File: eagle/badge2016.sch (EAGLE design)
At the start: 89 parts, among them IC1 25AA080SN, IC3 24AA01SN, J1 USB-MICRO, Q1_32.768KHZ NX5032G, Q2 BC857ALT1SMD, Q2_24MHZ NX5032G, X1 PASSER-07, X2 PASSER-07, X3 PASSER-07

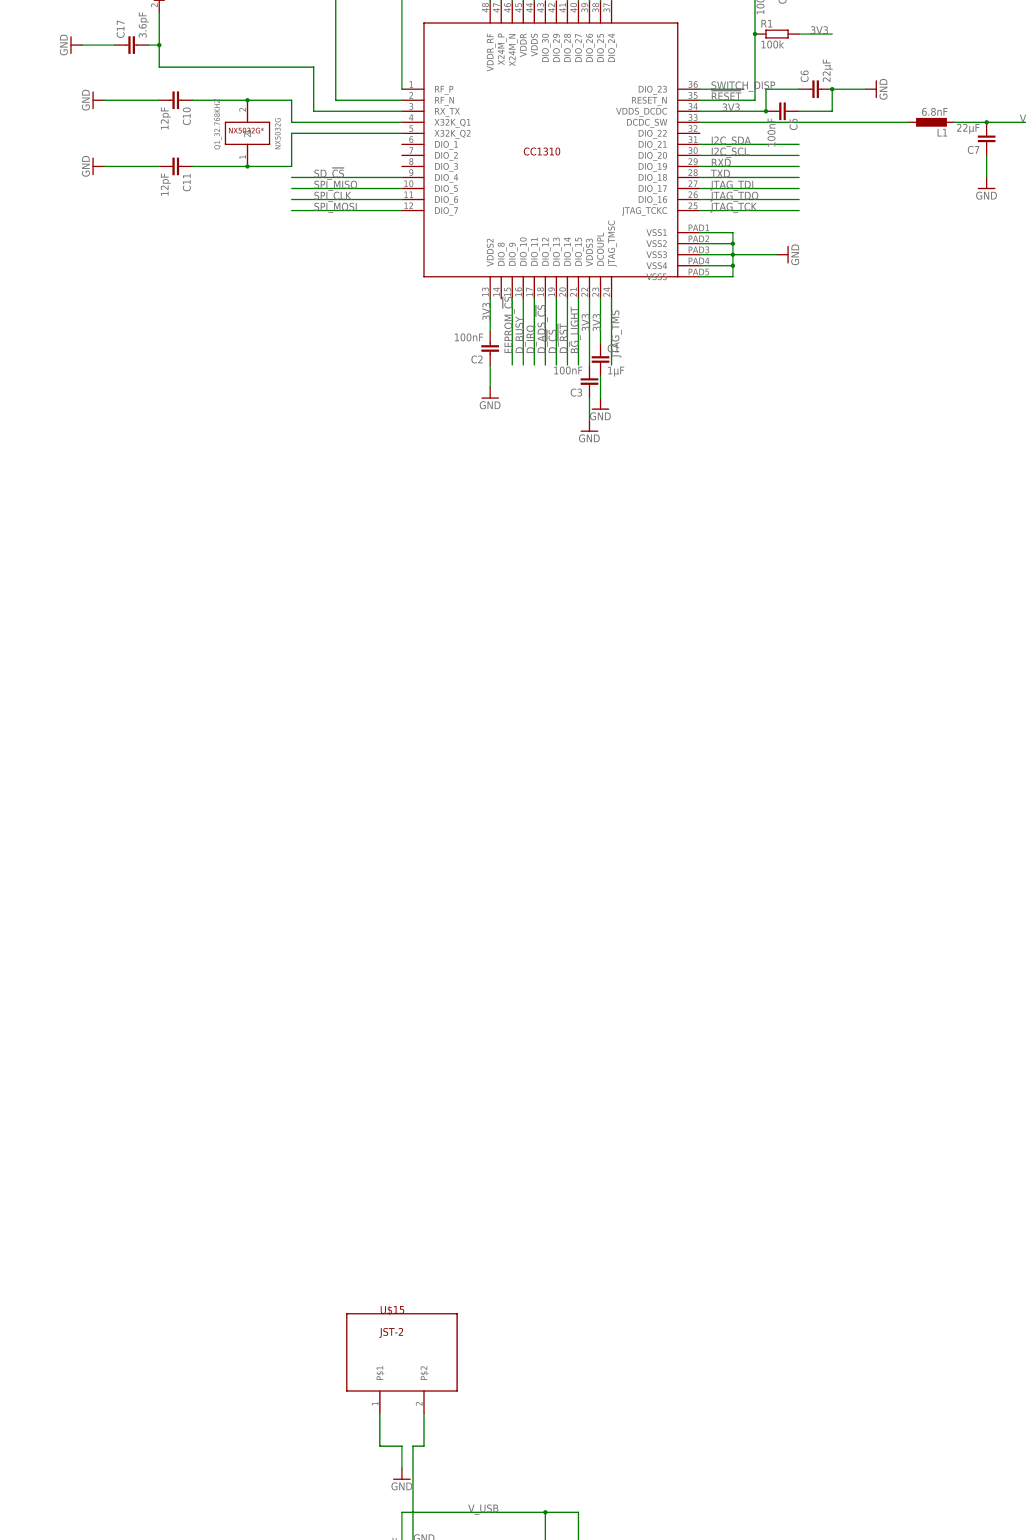
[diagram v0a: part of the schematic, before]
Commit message: fixed the inductor label (nF to nH) swapped 32khz crystal to different package + added package to lbr add pinhead to battery connector
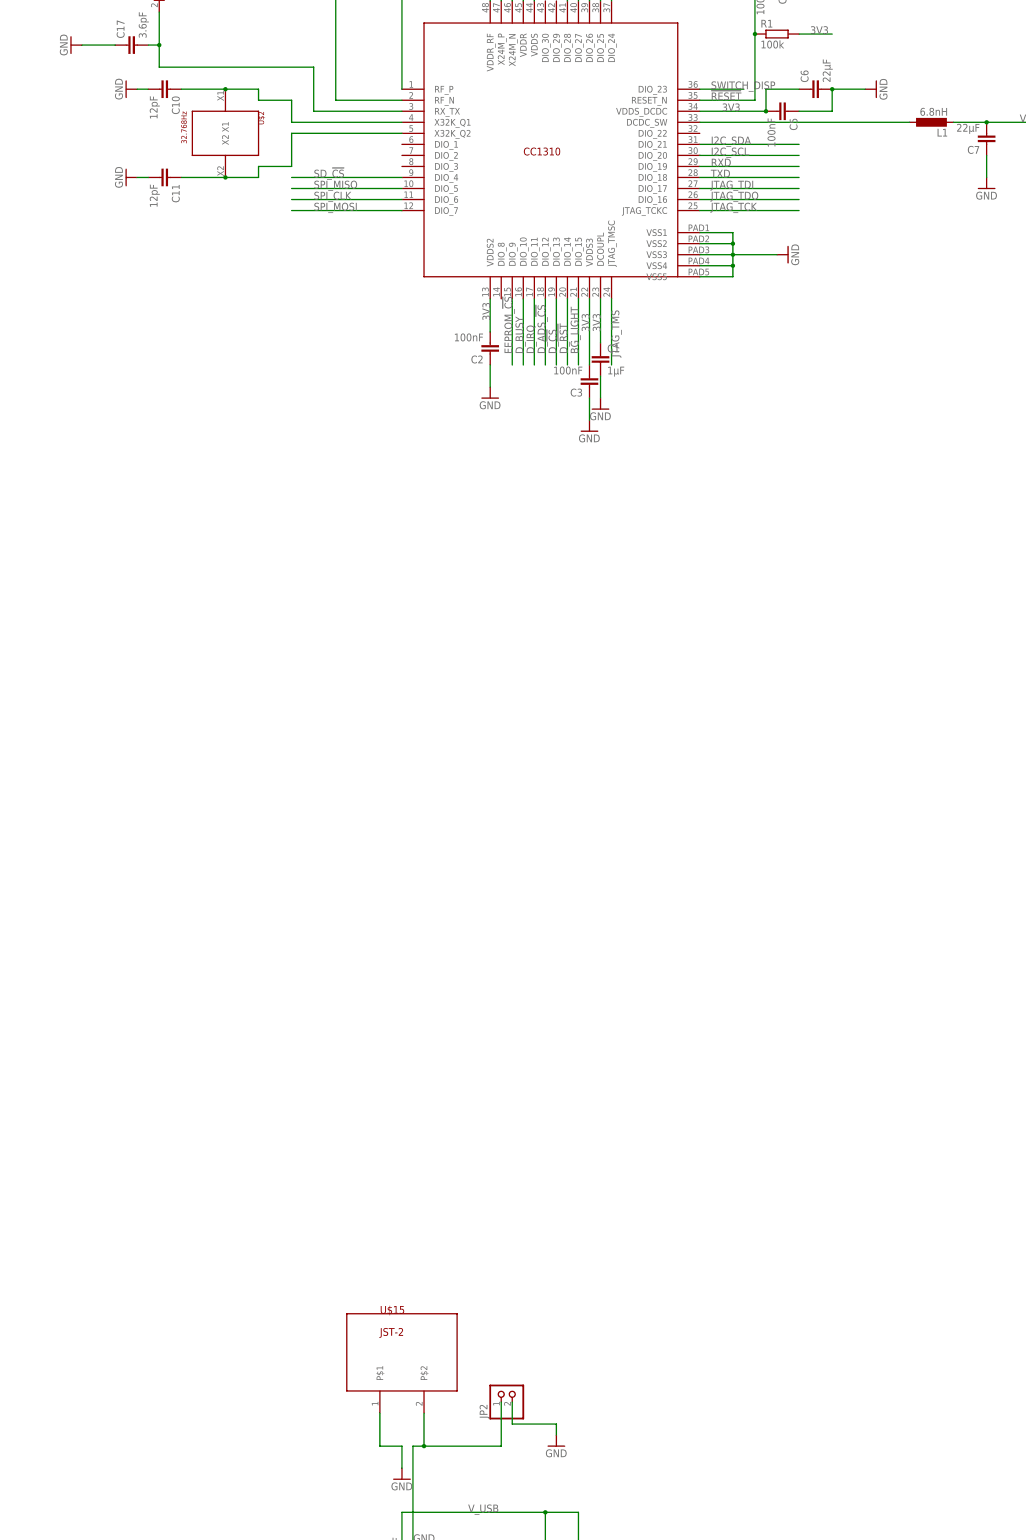
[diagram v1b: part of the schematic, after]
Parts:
- removed Q1_32.768KHZ: NX5032G, ERNW_parts:NX5032G
- added JP2: (no value), pinhead:PINHD-1X2
- added U$2: 32.768Hz, ERNW_parts:CMR200T
- L1: value 6.8nF -> 6.8nH
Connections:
- removed net N$1: C11.1, Q1_32.768KHZ.1, U$1.X32K_Q2
- new net N$16: C11.1, U$1.X32K_Q2, U$2.X2
- net GND: now also JP2.2
- net N$2: now also U$2.X1; no longer Q1_32.768KHZ.2
- net N$20: now also JP2.1
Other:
- moved on the sheet: C10, C11
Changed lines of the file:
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@@
 <part name="GND5" library="supply1" deviceset="GND" device=""/>
 <part name="GND6" library="supply1" deviceset="GND" device=""/>
-<part name="L1" library="rcl" deviceset="L-EU" device="L2012C" value="6.8nF"/>
+<part name="L1" library="rcl" deviceset="L-EU" device="L2012C" value="6.8nH"/>
 <part name="C6" library="rcl" deviceset="C-EU" device="C0603" value="22µF"/>
 <part name="C7" library="rcl" deviceset="C-EU" device="C0603" value="22µF"/>
@@
 <part name="GND8" library="supply1" deviceset="GND" device=""/>
 <part name="GND9" library="supply1" deviceset="GND" device=""/>
-<part name="Q1_32.768KHZ" library="ERNW_parts" deviceset="NX5032G*" device=""/>
 <part name="C10" library="rcl" deviceset="C-EU" device="C0402" value="12pF"/>
 <part name="C11" library="rcl" deviceset="C-EU" device="C0402" value="12pF"/>
@@
 <part name="R18" library="rcl" deviceset="R-EU_" device="R0402" value="NC"/>
 <part name="R21" library="rcl" deviceset="R-EU_" device="R0402" value="NC"/>
+<part name="U$2" library="ERNW_parts" deviceset="CMR200T" device="" value="32.768Hz"/>
+<part name="JP2" library="pinhead" deviceset="PINHD-1X2" device=""/>
+<part name="GND57" library="supply1" deviceset="GND" device=""/>
 </parts>
 <sheets>
@@
 <instance part="GND8" gate="1" x="43.18" y="104.14" rot="R180"/>
 <instance part="GND9" gate="1" x="50.8" y="116.84" rot="R180"/>
-<instance part="Q1_32.768KHZ" gate="G$1" x="-12.7" y="45.72" rot="R90"/>
-<instance part="C10" gate="G$1" x="-27.94" y="53.34" rot="R270"/>
-<instance part="C11" gate="G$1" x="-27.94" y="38.1" rot="R270"/>
-<instance part="GND10" gate="1" x="-48.26" y="53.34" rot="R270"/>
-<instance part="GND11" gate="1" x="-48.26" y="38.1" rot="R270"/>
+<instance part="C10" gate="G$1" x="-30.48" y="55.88" rot="R270"/>
+<instance part="C11" gate="G$1" x="-30.48" y="35.56" rot="R270"/>
+<instance part="GND10" gate="1" x="-40.64" y="55.88" rot="R270"/>
+<instance part="GND11" gate="1" x="-40.64" y="35.56" rot="R270"/>
 <instance part="Q2_24MHZ" gate="G$1" x="45.72" y="134.62" rot="R180"/>
 <instance part="C12" gate="G$1" x="38.1" y="157.48"/>
@@
 <instance part="R18" gate="G$1" x="226.06" y="-193.04" rot="R270"/>
 <instance part="R21" gate="G$1" x="233.68" y="-193.04" rot="R270"/>
+<instance part="U$2" gate="G$1" x="-17.78" y="45.72" rot="R270"/>
+<instance part="JP2" gate="G$1" x="48.26" y="-243.84" rot="R90"/>
+<instance part="GND57" gate="1" x="58.42" y="-256.54"/>
 </instances>
 <busses>
@@
 <pinref part="GND9" gate="1" pin="GND"/>
 <wire x1="50.8" y1="104.14" x2="50.8" y2="114.3" width="0.1524" layer="91"/>
-</segment>
-<segment>
-<pinref part="GND11" gate="1" pin="GND"/>
-<pinref part="C11" gate="G$1" pin="2"/>
-<wire x1="-45.72" y1="38.1" x2="-33.02" y2="38.1" width="0.1524" layer="91"/>
-</segment>
-<segment>
-<pinref part="C10" gate="G$1" pin="2"/>
-<pinref part="GND10" gate="1" pin="GND"/>
-<wire x1="-33.02" y1="53.34" x2="-45.72" y2="53.34" width="0.1524" layer="91"/>
 </segment>
 <segment>
@@
 <wire x1="287.02" y1="-91.44" x2="287.02" y2="-96.52" width="0.1524" layer="91"/>
 </segment>
+<segment>
+<pinref part="C11" gate="G$1" pin="2"/>
+<pinref part="GND11" gate="1" pin="GND"/>
+<wire x1="-35.56" y1="35.56" x2="-38.1" y2="35.56" width="0.1524" layer="91"/>
+</segment>
+<segment>
+<pinref part="C10" gate="G$1" pin="2"/>
+<pinref part="GND10" gate="1" pin="GND"/>
+<wire x1="-35.56" y1="55.88" x2="-38.1" y2="55.88" width="0.1524" layer="91"/>
+</segment>
+<segment>
+<pinref part="JP2" gate="G$1" pin="2"/>
+<wire x1="48.26" y1="-246.38" x2="48.26" y2="-251.46" width="0.1524" layer="91"/>
+<wire x1="48.26" y1="-251.46" x2="58.42" y2="-251.46" width="0.1524" layer="91"/>
+<pinref part="GND57" gate="1" pin="GND"/>
+<wire x1="58.42" y1="-251.46" x2="58.42" y2="-254" width="0.1524" layer="91"/>
+</segment>
 </net>
 <net name="3V3" class="0">
@@
 </segment>
 </net>
-<net name="N$1" class="0">
-<segment>
-<pinref part="U$1" gate="G$1" pin="X32K_Q2"/>
-<wire x1="22.86" y1="45.72" x2="-2.54" y2="45.72" width="0.1524" layer="91"/>
-<wire x1="-2.54" y1="45.72" x2="-2.54" y2="38.1" width="0.1524" layer="91"/>
-<pinref part="Q1_32.768KHZ" gate="G$1" pin="1"/>
-<wire x1="-2.54" y1="38.1" x2="-12.7" y2="38.1" width="0.1524" layer="91"/>
-<pinref part="C11" gate="G$1" pin="1"/>
-<wire x1="-25.4" y1="38.1" x2="-12.7" y2="38.1" width="0.1524" layer="91"/>
-<junction x="-12.7" y="38.1"/>
-</segment>
-</net>
 <net name="N$2" class="0">
 <segment>
@@
 <wire x1="22.86" y1="48.26" x2="-2.54" y2="48.26" width="0.1524" layer="91"/>
 <wire x1="-2.54" y1="48.26" x2="-2.54" y2="53.34" width="0.1524" layer="91"/>
-<pinref part="Q1_32.768KHZ" gate="G$1" pin="2"/>
-<wire x1="-2.54" y1="53.34" x2="-12.7" y2="53.34" width="0.1524" layer="91"/>
+<wire x1="-10.16" y1="55.88" x2="-10.16" y2="53.34" width="0.1524" layer="91"/>
+<wire x1="-10.16" y1="53.34" x2="-2.54" y2="53.34" width="0.1524" layer="91"/>
+<pinref part="U$2" gate="G$1" pin="X1"/>
+<wire x1="-10.16" y1="55.88" x2="-17.78" y2="55.88" width="0.1524" layer="91"/>
 <pinref part="C10" gate="G$1" pin="1"/>
-<wire x1="-12.7" y1="53.34" x2="-25.4" y2="53.34" width="0.1524" layer="91"/>
-<junction x="-12.7" y="53.34"/>
+<wire x1="-17.78" y1="55.88" x2="-27.94" y2="55.88" width="0.1524" layer="91"/>
+<junction x="-17.78" y="55.88"/>
 </segment>
 </net>
@@
 <wire x1="25.4" y1="-256.54" x2="27.94" y2="-256.54" width="0.1524" layer="91"/>
 <wire x1="27.94" y1="-256.54" x2="27.94" y2="-248.92" width="0.1524" layer="91"/>
+<pinref part="JP2" gate="G$1" pin="1"/>
+<wire x1="27.94" y1="-256.54" x2="45.72" y2="-256.54" width="0.1524" layer="91"/>
+<wire x1="45.72" y1="-256.54" x2="45.72" y2="-246.38" width="0.1524" layer="91"/>
+<junction x="27.94" y="-256.54"/>
 </segment>
 </net>
@@
 </segment>
 </net>
+<net name="N$16" class="0">
+<segment>
+<pinref part="C11" gate="G$1" pin="1"/>
+<pinref part="U$2" gate="G$1" pin="X2"/>
+<wire x1="-27.94" y1="35.56" x2="-17.78" y2="35.56" width="0.1524" layer="91"/>
+<pinref part="U$1" gate="G$1" pin="X32K_Q2"/>
+<wire x1="22.86" y1="45.72" x2="-2.54" y2="45.72" width="0.1524" layer="91"/>
+<wire x1="-2.54" y1="45.72" x2="-2.54" y2="38.1" width="0.1524" layer="91"/>
+<wire x1="-10.16" y1="35.56" x2="-10.16" y2="38.1" width="0.1524" layer="91"/>
+<wire x1="-10.16" y1="38.1" x2="-2.54" y2="38.1" width="0.1524" layer="91"/>
+<wire x1="-17.78" y1="35.56" x2="-10.16" y2="35.56" width="0.1524" layer="91"/>
+<junction x="-17.78" y="35.56"/>
+</segment>
+</net>

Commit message: fixed PCB with design
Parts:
- removed C36: 4.7µF, rcl:C-EUC0402
- removed R15, R18, R21: NC, rcl:R-EU_R0402
- removed R16, R17: 10k, rcl:R-EU_R0402
- removed R2_NC: 0, rcl:R-EU_R0402
- removed U$12: FT231X, ERNW_parts:FT231X
- added IC2: FT231XQ, we-chip:FT231XQ
- added LOGO1: LOGO-S_LAYER, we-symbol:LOGO-S_LAYER
- added NC-R15, NC-R18, NC-R21: NC, we-rcl:RESISTOR-0402
- added NC-R16, NC-R17: 10k, we-rcl:RESISTOR-0402
- added NC_C35: 100nF, we-rcl:CAPACITOR-0402
- added NC_C36: 4.7µF, we-rcl:CAPACITOR-0402
- added NC_LED2: (no value), we-opto:LED-0603
- added NC_R15, NC_R16, NC_R2, NC_R3: 0, we-rcl:RESISTOR-0603
- added NC_R5: 1k5, we-rcl:RESISTOR-0402
- added U$3: BB_TEST, ERNW_parts:BB_TEST
- added U$4: MESSAGE, ERNW_parts:MESSAGE
- added U$5: TR_BRAILLE, ERNW_parts:TR_BRAILLE
- added U$6: TR_PIGPEN, ERNW_parts:TR_PIGPEN
- added X10, X11, X12, X13, X14, X15, X16, X17, X18, X19, X20, X8, X9: PAD-1.27X1.27, we-rcl:PAD-1.27X1.27
- added X4, X5, X6, X7: PAD-0.5, we-rcl:PAD-0.5
- C1: device rcl:C-EUC0603 -> we-rcl:CAPACITOR-0402
- C10, C11, C12, C13, C14, C15, C16, C17, C18, C19, C2, C20, C21, C22, C25, C26, C3, C30, C31, C32, C33, C34, C4, C5, C8, C9: device rcl:C-EUC0402 -> we-rcl:CAPACITOR-0402
- C23, C24, C27, C28: device rcl:C-EUC0805 -> we-rcl:CAPACITOR-0805
- C29: device rcl:C-EUC0805 -> we-rcl:CAPACITOR-0603
- C35: value 100nF -> 2.2µF; device rcl:C-EUC0402 -> we-rcl:CAPACITOR-0603
- C6, C7: device rcl:C-EUC0603 -> we-rcl:CAPACITOR-0603
- L1: value 6.8nH -> 6.8µH; device rcl:L-EUL2012C -> we-rcl:INDUCTOR-0402
- L4, L5, L6, L7, L8, L9: device ERNW_parts:L_0402 -> we-rcl:INDUCTOR-0402
- LED1: device led:LEDCHIP-LED0603 -> we-opto:LED-0603
- R1, R10, R11, R12, R13, R14, R19, R2, R20, R4, R5, R6, R7, R9: device rcl:R-EU_R0402 -> we-rcl:RESISTOR-0402
- R3: value 0 -> 100k; device rcl:R-EU_R0402 -> we-rcl:RESISTOR-0402
- R8: value (none) -> 1k; device rcl:R-EU_R0402 -> we-rcl:RESISTOR-0402
- renumbered IC3 to NC-IC3, JP1 to NC-JP1, JP2 to NC-JP2, JP4 to NC-JP4, JTAG to NC-JTAG, SD1 to NC-SD1, U$10 to NC-U$10, U$13 to NC-U$13, UART to NC-UART
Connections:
- new net N$1: IC2.!RTS
- new net N$19: C1.1, U$1.DCOUPL
- new net N$21: IC2.!CTS
- new net N$24: IC2.!DTR
- new net N$26: IC2.!DSR
- new net N$31: IC2.!DCD
- new net N$34: IC2.!RI
- new net N$35: U$1.DIO_22, X5.P
- new net N$36: U$1.DIO_21, X6.P
- new net N$38: U$1.DIO_20, X7.P
- new net N$39: IC2.CBUS3, NC_R5.1, X17.P
- new net N$40: NC_LED2.A, NC_R5.2
- new net N$41: U$11.!ON, X20.P
- new net SWITCH_DISP_2: C35.2, R3.2, U$11.PWR_ON2
- net !BCD: now also IC2.CBUS0; no longer U$12.CBUS0
- net !PWREN: now also IC2.RXLED/CBUS1; no longer U$12.CBUS1
- net !SLEEP: now also IC2.TXLED/CBUS2, X16.P; no longer U$12.CBUS2
- net 3V3: now also NC-R15.1, NC-R16.1, NC-R17.1, NC-R18.1, NC-R21.1, NC_C35.2, NC_C36.2, NC_R16.1, NC_R16.2, X13.P; no longer C1.1, C35.2, C36.2, R15.1, R16.1, R17.1, R18.1, R21.1, U$1.DCOUPL
- net BG_LIGHT: now also X19.P
- net DM: now also IC2.USBDM; no longer U$12.USBDM
- net DP: now also IC2.USBDP; no longer U$12.USBDP
- net GND: now also IC2.GND, NC_C35.1, NC_C36.1, NC_LED2.C, U$15.P$2, X11.P; no longer C36.1, U$11.!ON, U$12.GND0, U$12.GND1, U$12.GND2, U$15.P$1
- net I2C_SCL: now also NC-R17.2, U$1.DIO_18; no longer R17.2, U$1.DIO_20
- net I2C_SDA: now also NC-R16.2, U$1.DIO_19; no longer R16.2, U$1.DIO_21
- net LED_A: now also X18.P
- net N$14: now also U$1.DIO_1, X4.P; no longer C21.1, R2_NC.2, R3.1
- net N$15: now also C21.1, NC_R2.2, NC_R3.1, NC_R3.2; no longer R3.2
- net N$17: now also NC_R2.1; no longer R2_NC.1
- net N$20: now also U$15.P$1; no longer U$15.P$2
- net N$25: now also X8.P
- net N$32: now also X9.P
- net N$37: now also IC2.!RESET, IC2.3V3OUT, IC2.VCCIO; no longer U$12.!RESET, U$12.3V3OUT, U$12.VCCIO
- net PROG: now also X15.P
- net RXD: now also IC2.RXD, U$1.DIO_2; no longer U$1.DIO_19, U$12.RXD
- net SD_D1: now also NC-R18.2; no longer R18.2
- net SD_D2: now also NC-R15.2; no longer R15.2
- net SPI_MISO: now also NC-R21.2; no longer R21.2
- net SWITCH_DISP: now also R3.1; no longer U$11.PWR_ON2
- net TXD: now also IC2.TXD, U$1.DIO_3; no longer U$1.DIO_18, U$12.TXD
- net VDDR: now also X14.P
- net VUSB_IN: now also IC2.VCC, X10.P; no longer U$12.VCC
- net V_DISP: now also NC_R15.1, NC_R15.2, X12.P

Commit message: Update badge2016.sch
Change RX <-> TX for UART
Add additional "pad" for DIO_8
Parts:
- added R15, R16: 0, we-rcl:RESISTOR-0402
- added X21: PAD-0.5, we-rcl:PAD-0.5
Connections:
- new net N$53: U$1.DIO_8, X21.P
- new net UART_RXD: R15.1, U$1.DIO_2
- new net UART_TXD: R16.1, U$1.DIO_3
- net RXD: now also R16.2; no longer U$1.DIO_2
- net TXD: now also R15.2; no longer U$1.DIO_3
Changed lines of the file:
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@@
 <?xml version="1.0" encoding="utf-8"?>
 <!DOCTYPE eagle SYSTEM "eagle.dtd">
-<eagle version="7.5.0">
+<eagle version="7.3.0">
 <drawing>
 <settings>
@@
 <part name="C35" library="we-rcl" deviceset="CAPACITOR" device="-0603" value="2.2µF"/>
 <part name="GND28" library="supply1" deviceset="GND" device=""/>
+<part name="X21" library="we-rcl" deviceset="PAD" device="-0.5"/>
+<part name="R15" library="we-rcl" deviceset="RESISTOR" device="-0402" value="0"/>
+<part name="R16" library="we-rcl" deviceset="RESISTOR" device="-0402" value="0"/>
 </parts>
 <sheets>
@@
 <instance part="C35" gate="C" x="12.7" y="-386.08"/>
 <instance part="GND28" gate="1" x="-7.62" y="-386.08" rot="R270"/>
+<instance part="X21" gate="X" x="45.72" y="-10.16" rot="R90"/>
+<instance part="R15" gate="R" x="-185.42" y="-436.88" rot="R180"/>
+<instance part="R16" gate="R" x="-177.8" y="-439.42" rot="R180"/>
 </instances>
 <busses>
@@
 <net name="TXD" class="0">
 <segment>
+<pinref part="IC2" gate="IC" pin="TXD"/>
+<wire x1="-205.74" y1="-436.88" x2="-190.5" y2="-436.88" width="0.1524" layer="91"/>
+<label x="-200.66" y="-436.88" size="1.778" layer="95"/>
+<pinref part="R15" gate="R" pin="2"/>
+</segment>
+<segment>
 <pinref part="NC-UART" gate="A" pin="4"/>
 <wire x1="187.96" y1="251.46" x2="223.52" y2="251.46" width="0.1524" layer="91"/>
 <label x="193.04" y="251.46" size="1.778" layer="95"/>
-</segment>
-<segment>
-<pinref part="IC2" gate="IC" pin="TXD"/>
-<wire x1="-205.74" y1="-436.88" x2="-190.5" y2="-436.88" width="0.1524" layer="91"/>
-<label x="-200.66" y="-436.88" size="1.778" layer="95"/>
-</segment>
-<segment>
-<pinref part="U$1" gate="G$1" pin="DIO_3"/>
-<wire x1="22.86" y1="38.1" x2="0" y2="38.1" width="0.1524" layer="91"/>
-<label x="2.54" y="38.1" size="1.778" layer="95"/>
-</segment>
-</net>
-<net name="RXD" class="0">
-<segment>
-<pinref part="NC-UART" gate="A" pin="5"/>
-<wire x1="187.96" y1="248.92" x2="223.52" y2="248.92" width="0.1524" layer="91"/>
-<label x="193.04" y="248.92" size="1.778" layer="95"/>
-</segment>
-<segment>
-<pinref part="IC2" gate="IC" pin="RXD"/>
-<wire x1="-205.74" y1="-439.42" x2="-190.5" y2="-439.42" width="0.1524" layer="91"/>
-<label x="-200.66" y="-439.42" size="1.778" layer="95"/>
-</segment>
-<segment>
-<pinref part="U$1" gate="G$1" pin="DIO_2"/>
-<wire x1="22.86" y1="40.64" x2="0" y2="40.64" width="0.1524" layer="91"/>
-<label x="2.54" y="40.64" size="1.778" layer="95"/>
 </segment>
 </net>
@@
 <pinref part="X5" gate="X" pin="P"/>
 <wire x1="91.44" y1="45.72" x2="111.76" y2="45.72" width="0.1524" layer="91"/>
+<wire x1="114.3" y1="45.72" x2="111.76" y2="45.72" width="0.1524" layer="91"/>
 </segment>
 </net>
@@
 </segment>
 </net>
+<net name="N$53" class="0">
+<segment>
+<pinref part="U$1" gate="G$1" pin="DIO_8"/>
+<wire x1="45.72" y1="7.62" x2="45.72" y2="-7.62" width="0.1524" layer="91"/>
+<pinref part="X21" gate="X" pin="P"/>
+</segment>
+</net>
+<net name="RXD" class="0">
+<segment>
+<pinref part="IC2" gate="IC" pin="RXD"/>
+<wire x1="-205.74" y1="-439.42" x2="-182.88" y2="-439.42" width="0.1524" layer="91"/>
+<label x="-200.66" y="-439.42" size="1.778" layer="95"/>
+<pinref part="R16" gate="R" pin="2"/>
+</segment>
+<segment>
+<pinref part="NC-UART" gate="A" pin="5"/>
+<wire x1="187.96" y1="248.92" x2="223.52" y2="248.92" width="0.1524" layer="91"/>
+<label x="193.04" y="248.92" size="1.778" layer="95"/>
+</segment>
+</net>
+<net name="UART_RXD" class="0">
+<segment>
+<pinref part="U$1" gate="G$1" pin="DIO_2"/>
+<wire x1="22.86" y1="40.64" x2="0" y2="40.64" width="0.1524" layer="91"/>
+<label x="2.54" y="40.64" size="1.778" layer="95"/>
+</segment>
+<segment>
+<pinref part="R15" gate="R" pin="1"/>
+<wire x1="-180.34" y1="-436.88" x2="-165.1" y2="-436.88" width="0.1524" layer="91"/>
+</segment>
+</net>
+<net name="UART_TXD" class="0">
+<segment>
+<pinref part="U$1" gate="G$1" pin="DIO_3"/>
+<wire x1="22.86" y1="38.1" x2="0" y2="38.1" width="0.1524" layer="91"/>
+<label x="2.54" y="38.1" size="1.778" layer="95"/>
+</segment>
+<segment>
+<pinref part="R16" gate="R" pin="1"/>
+<wire x1="-172.72" y1="-439.42" x2="-165.1" y2="-439.42" width="0.1524" layer="91"/>
+</segment>
+</net>
